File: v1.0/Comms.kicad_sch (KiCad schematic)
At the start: 9 parts, among them J3 USB_C_Receptacle_USB2.0_16P, J4 SWD, J5 Conn_01x04, U8 USBLC6-2SC6

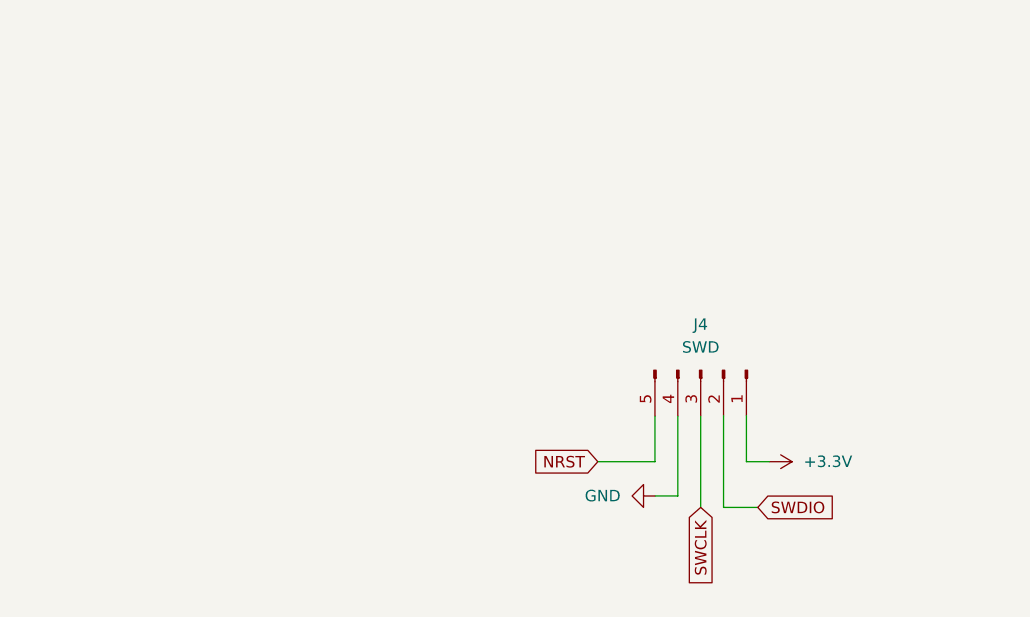
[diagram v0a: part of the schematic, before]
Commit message: v1.0: update schematics and PCB layout
Co-Authored-By: Claude Opus 4.7 (1M context) <noreply@anthropic.com>
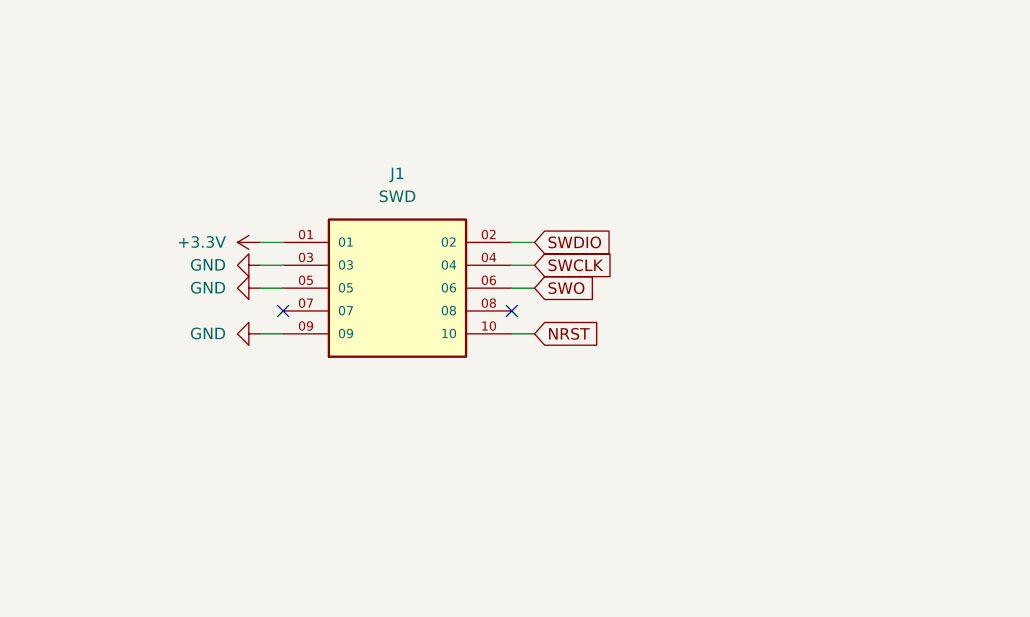
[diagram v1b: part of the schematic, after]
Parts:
- removed J4: SWD, Connector_PinHeader_2.54mm:PinHeader_1x05_P2.54mm_Vertical, symbol Connector:Conn_01x05_Pin
- added J1: SWD, UNSW_ROCKETRY_LIBRARY:SAMTEC_FTSH-105-01-X-DV-K-X, symbol UNSW_ROCKETRY_LIBRARY:FTSH-105-01-X-DV-K-X
- J5: footprint Connector_PinHeader_2.54mm:PinHeader_1x04_P2.54mm_Vertical -> Connector_Molex:Molex_PicoBlade_53047-0410_1x04_P1.25mm_Vertical
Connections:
- net +3.3V: now also J1.01
- net GND: now also J1.03, J1.05, J1.09
- net NRST: now also J1.10
- net SWCLK: now also J1.04
- net SWDIO: now also J1.02
- new net SWO: J1.06
- no-connect marks 2 -> 4
